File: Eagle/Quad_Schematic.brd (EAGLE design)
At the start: 100 x 80 mm, 36 parts, among them J1 FTDI_DEVICE, M1 WIRELESS-NRF24L01, U1 ATMEGA328P_TQFP, U2 GY-521MPU6050

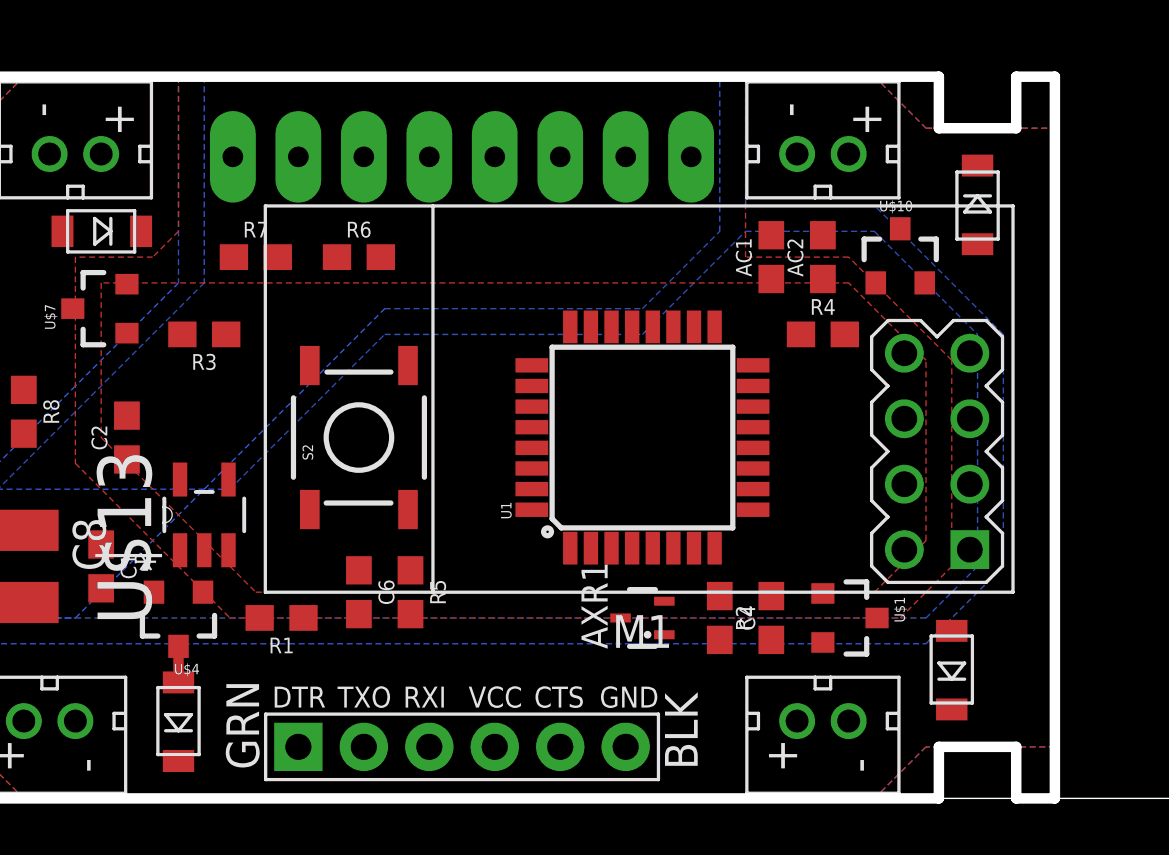
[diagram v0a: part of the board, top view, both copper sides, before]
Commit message: kinda more optimized, but not a lot of traces done.
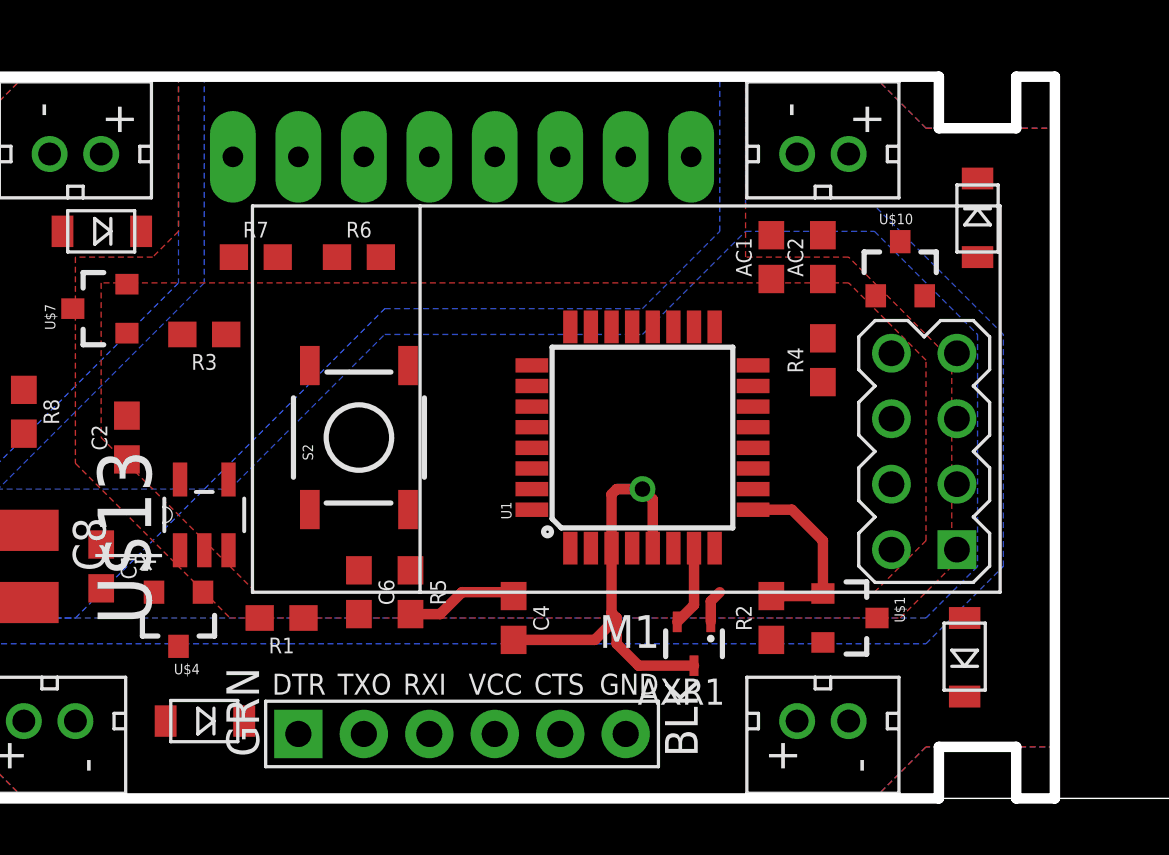
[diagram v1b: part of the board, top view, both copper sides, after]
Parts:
- moved C4 8.00 mm to (26.0, 7.00)
- moved AXR1 2.24 mm to (33.0, 6.00), turned to 180 degrees
- moved R4 1.00 mm to (38.0, 17.0), turned to 90 degrees
- moved U$6 1.00 mm to (14.0, 3.00), turned to 270 degrees
- moved U$3 0.71 mm to (43.5, 5.50)
- moved J1 0.50 mm to (24.0, 2.50)
- moved M1 0.50 mm to (30.5, 16.0)
- moved U$10 0.50 mm to (41.0, 20.5)
- moved U$12 0.50 mm to (44.0, 22.5)
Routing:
- net GND: track 0.00 -> 18.3 mm, vias 0 -> 1
- net M1: track 0.00 -> 7.35 mm
- net 3V3: track 0.00 -> 5.71 mm
- net OSC1: track 0.00 -> 3.13 mm
- net N$5: track 1.40 -> 0.00 mm

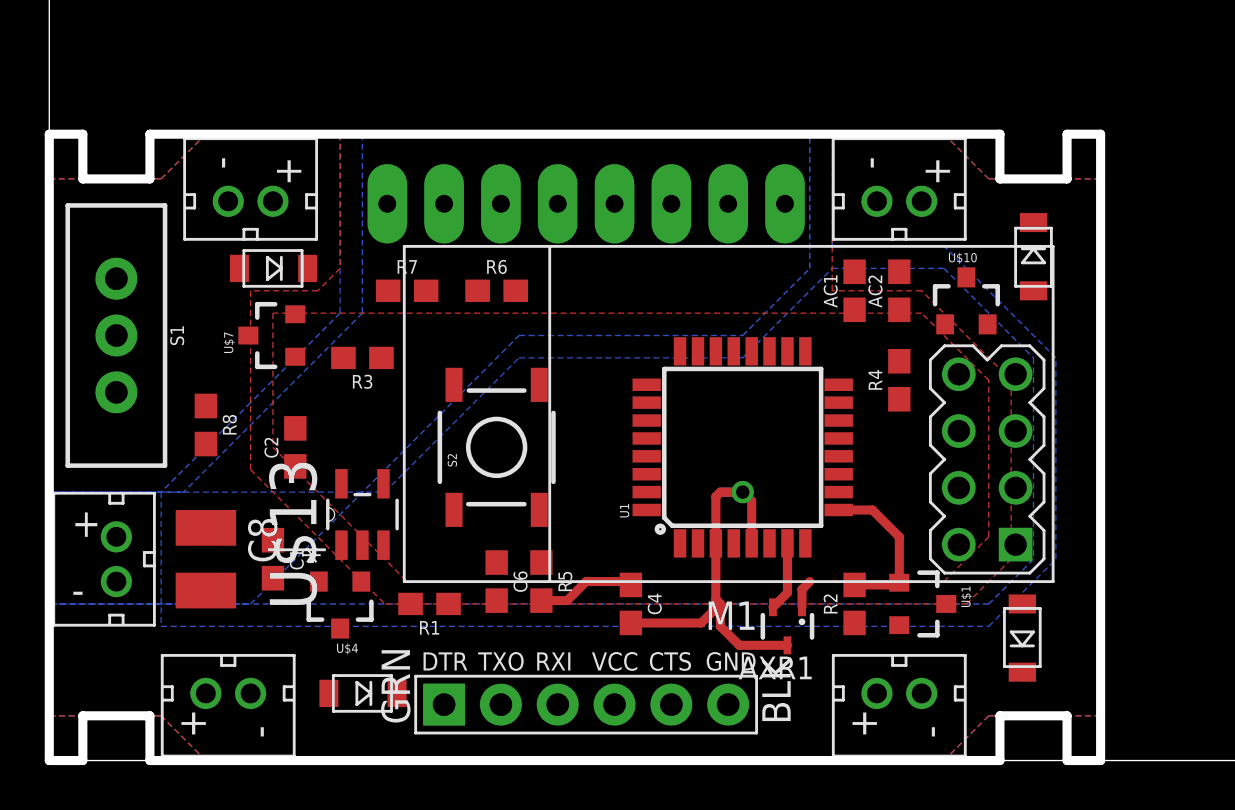
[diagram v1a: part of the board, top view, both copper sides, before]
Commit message: 23 airwires left
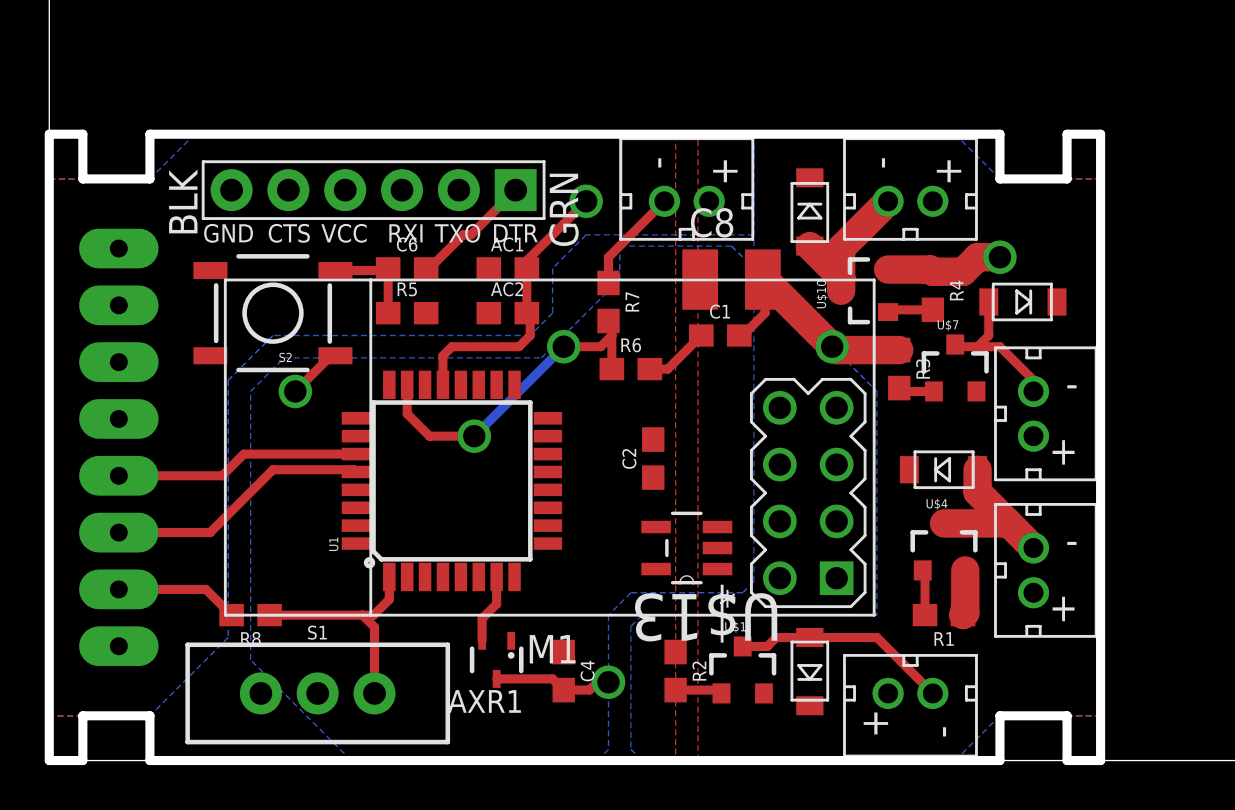
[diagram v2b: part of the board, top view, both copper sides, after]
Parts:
- moved U$5 36.4 mm to (44.0, 8.50), turned to 180 degrees
- moved U$8 36.3 mm to (44.0, 15.5), turned to 180 degrees
- moved U$9 33.5 mm to (43.5, 20.5)
- moved U$7 30.5 mm to (40.5, 17.5), turned to 0 degrees
- moved BATT 30.1 mm to (28.5, 25.0), turned to 270 degrees
- moved U$6 27.9 mm to (40.0, 13.0), turned to 90 degrees
- moved U$4 27.1 mm to (40.0, 9.50), turned to 0 degrees
- moved C8 26.6 mm to (30.5, 21.5), turned to 0 degrees
- moved J1 24.9 mm to (14.5, 25.5), turned to 180 degrees
- moved R3 24.0 mm to (38.0, 17.5), turned to 270 degrees
- moved R1 23.0 mm to (40.0, 6.50)
- moved C1 22.4 mm to (30.0, 19.0), turned to 0 degrees
- moved S1 18.4 mm to (12.0, 3.00), turned to 270 degrees
- moved AC2 17.5 mm to (20.5, 20.0), turned to 0 degrees
- moved C2 16.0 mm to (27.0, 13.5)
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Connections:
- net BATT_CHECK: now also U1.23; no longer U1.26
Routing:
- net GND: track 18.3 -> 48.5 mm, vias 1 -> 5
- net BATT_CHECK: track 0.00 -> 14.9 mm, vias 0 -> 2
- net SCL: track 0.00 -> 11.8 mm
- net SDA: track 0.00 -> 11.0 mm
- net SWITCH: track 0.00 -> 10.4 mm
- net N$1: track 0.00 -> 9.70 mm
- net N$8: track 0.00 -> 8.97 mm
- net N$5: track 0.00 -> 7.44 mm
- net N$10: track 0.00 -> 6.87 mm
- net 3V3: track 5.71 -> 0.00 mm
- net DTR: track 0.00 -> 5.45 mm
- net M1: track 7.35 -> 2.11 mm
- net RESET: track 0.00 -> 4.40 mm
- net MVCC: track 0.00 -> 2.92 mm
- net M2: track 0.00 -> 2.04 mm
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
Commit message: the first submission
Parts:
- moved R6 4.03 mm to (25.5, 21.5), turned to 90 degrees
- moved C1 2.55 mm to (27.5, 18.5)
- moved C2 1.80 mm to (28.5, 12.5), turned to 0 degrees
- moved C8 1.58 mm to (29.0, 21.0)
- moved R7 1.41 mm to (24.0, 21.5)
- moved R2 1.00 mm to (28.0, 3.00)
- moved R4 0.50 mm to (39.0, 21.0)
- moved U$1 0.50 mm to (31.0, 4.50)
- moved U$12 0.50 mm to (34.5, 24.5)
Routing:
- net GND: track 48.5 -> 82.3 mm, vias 5 -> 11
- net M3: track 1.61 -> 32.3 mm, vias 0 -> 2
- net M4: track 2.04 -> 31.7 mm, vias 0 -> 2
- net M2: track 2.04 -> 29.9 mm, vias 0 -> 2
- net TX0: track 0.00 -> 27.4 mm, vias 0 -> 3
- net RXI: track 0.00 -> 23.9 mm, vias 0 -> 2
- net CE: track 0.00 -> 23.5 mm, vias 0 -> 1
- net INT: track 0.00 -> 23.0 mm, vias 0 -> 3
- net SCK: track 0.00 -> 21.8 mm, vias 0 -> 1
- net RESET: track 4.40 -> 24.1 mm, vias 0 -> 2
- net CS: track 0.00 -> 18.1 mm, vias 0 -> 1
- net MISO: track 0.00 -> 14.9 mm
- net M1: track 2.11 -> 14.9 mm, vias 0 -> 2
- net MOSI: track 0.00 -> 11.7 mm, vias 0 -> 1
- net MVCC: track 2.92 -> 10.0 mm
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
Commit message: 2 airwires left
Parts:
- moved U$13 12.5 mm to (23.5, 21.0), turned to 270 degrees
- moved C2 6.00 mm to (28.5, 6.50)
- moved AC1 4.74 mm to (19.0, 17.5), flipped to the bottom, turned to 90 degrees
- moved AC2 3.91 mm to (17.5, 17.5), flipped to the bottom, turned to 90 degrees
- moved R7 3.04 mm to (23.5, 18.5), flipped to the bottom, turned to 0 degrees
- moved R6 2.24 mm to (23.5, 20.5), flipped to the bottom, turned to 180 degrees
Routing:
- net M3: track 32.3 -> 1.61 mm, vias 2 -> 0
- net M4: track 31.7 -> 1.54 mm, vias 2 -> 0
- net GND: track 82.3 -> 73.6 mm, vias 11 -> 12
- net 3V3: track 0.00 -> 6.57 mm, vias 0 -> 1
- net MVCC: track 10.0 -> 3.97 mm, vias 0 -> 1
- net CS: track 18.1 -> 15.1 mm, vias 1 -> 2
- net BATT_CHECK: track 17.0 -> 14.2 mm, vias 2 -> 1
- net SCK: track 21.8 -> 24.3 mm
- net MISO: track 14.9 -> 16.2 mm, vias 0 -> 1
- net MOSI: track 11.7 -> 11.1 mm
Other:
- board size 100 x 80 mm -> 47 x 28 mm

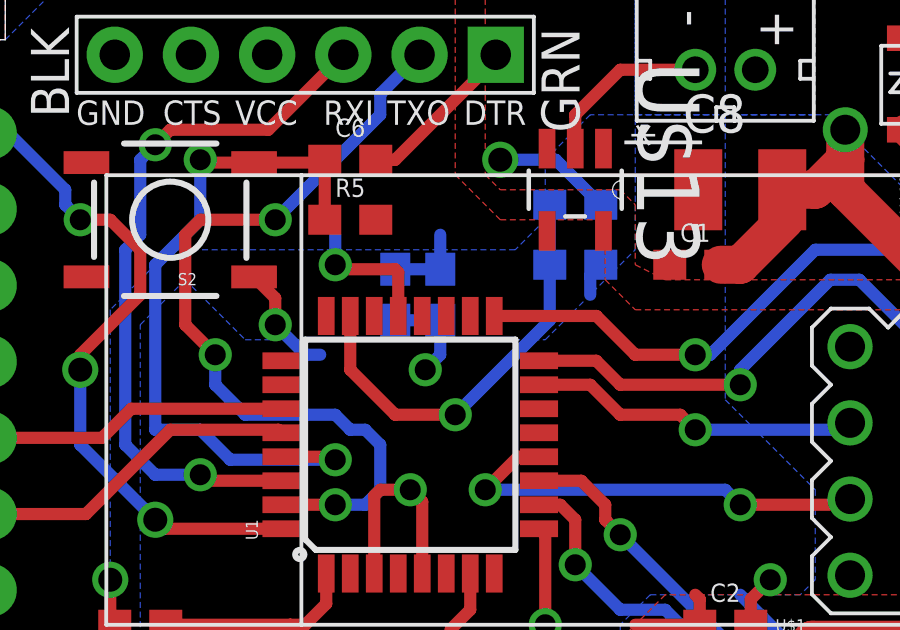
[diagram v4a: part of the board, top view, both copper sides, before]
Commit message: moved batt_check
also rip
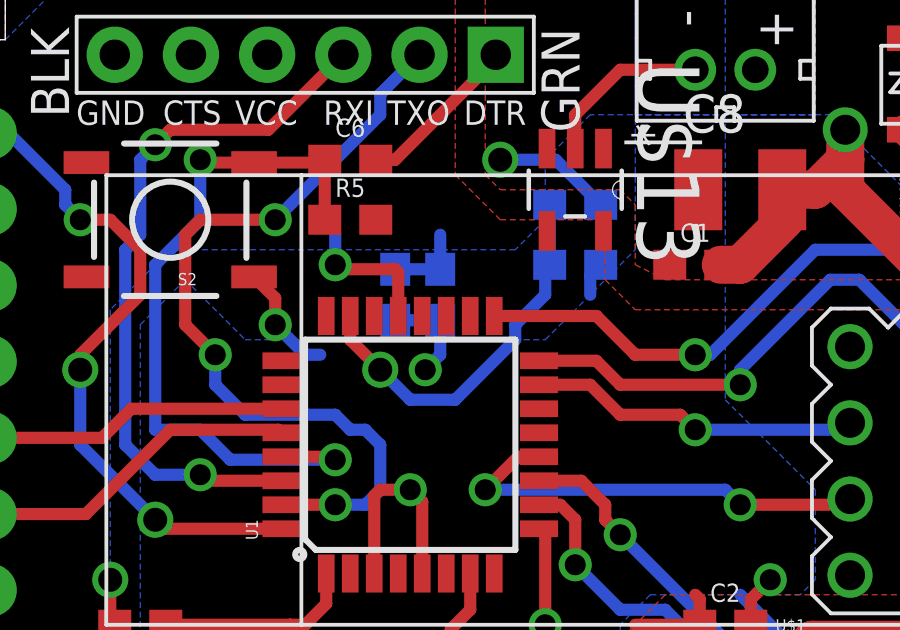
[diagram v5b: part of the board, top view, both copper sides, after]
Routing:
- net BATT_CHECK: track 14.2 -> 12.9 mm
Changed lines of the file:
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@@
 <grid distance="0.5" unitdist="mm" unit="mm" style="lines" multiple="1" display="yes" altdistance="0.5" altunitdist="mm" altunit="mm"/>
 <layers>
-<layer number="1" name="Top" color="4" fill="1" visible="no" active="yes"/>
+<layer number="1" name="Top" color="4" fill="1" visible="yes" active="yes"/>
 <layer number="16" name="Bottom" color="1" fill="1" visible="yes" active="yes"/>
 <layer number="17" name="Pads" color="2" fill="1" visible="yes" active="yes"/>
@@
 <contactref element="R6" pad="1"/>
 <contactref element="U1" pad="23"/>
-<wire x1="22.65" y1="20.5" x2="22.65" y2="18.5" width="0.4064" layer="16"/>
-<wire x1="22.65" y1="18.5" x2="22.65" y2="16.65" width="0.4064" layer="16"/>
-<wire x1="22.65" y1="16.65" x2="19.5" y2="13.5" width="0.4064" layer="16"/>
-<via x="19.5" y="13.5" extent="1-16" drill="0.7"/>
-<wire x1="16" y1="15" x2="16" y2="16.7926" width="0.4064" layer="1"/>
-<wire x1="19.5" y1="13.5" x2="17.5" y2="13.5" width="0.4064" layer="1"/>
-<wire x1="17.5" y1="13.5" x2="16" y2="15" width="0.4064" layer="1"/>
+<wire x1="22.65" y1="18.5" x2="22.65" y2="20.5" width="0.4064" layer="16"/>
+<wire x1="16" y1="16.7926" x2="16" y2="16" width="0.4064" layer="1"/>
+<wire x1="16" y1="16" x2="17" y2="15" width="0.4064" layer="1"/>
+<via x="17" y="15" extent="1-16" drill="0.8"/>
+<wire x1="17" y1="15" x2="18" y2="14" width="0.4064" layer="16"/>
+<wire x1="18" y1="14" x2="19.5" y2="14" width="0.4064" layer="16"/>
+<wire x1="19.5" y1="14" x2="21.5" y2="16" width="0.4064" layer="16"/>
+<wire x1="21.5" y1="16" x2="21.5" y2="16.5" width="0.4064" layer="16"/>
+<wire x1="21.5" y1="16.5" x2="22.5" y2="17.5" width="0.4064" layer="16"/>
+<wire x1="22.5" y1="17.5" x2="22.5" y2="18.35" width="0.4064" layer="16"/>
+<wire x1="22.5" y1="18.35" x2="22.65" y2="18.5" width="0.4064" layer="16"/>
 </signal>
 <signal name="DTR">
